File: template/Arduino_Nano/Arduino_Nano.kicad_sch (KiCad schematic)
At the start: 6 parts, among them P1 Digital, P2 Analog, P3 CONN_01X01, P4 CONN_01X01, P5 CONN_01X01, P6 CONN_01X01

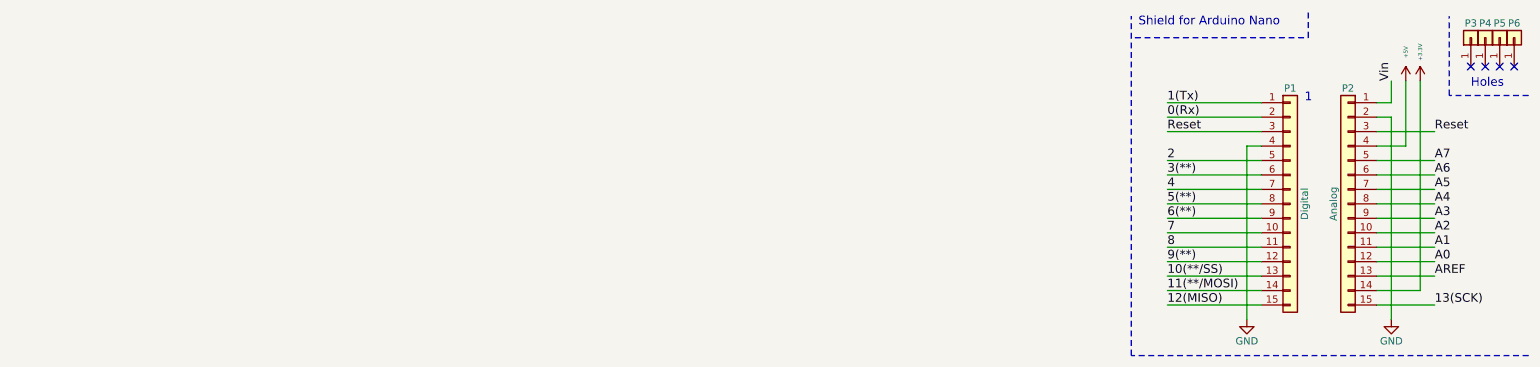
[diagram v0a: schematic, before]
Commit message: fix: change original libs; add: new components
- Fix LIS3DH pins positions;
- Add ATmega164P symbol;
- Add 3D model to the L_Wuerth_HCM-7050;
- Add parameters for R_RES (Assembly...).
- Add parameters for R_RES and C_CAP;
- Fix SOIC-8 package 3D model;
- Add new parameters for many symbols;
- Change text height from 70 mil to 50 mil;
- Add solder mask expansion for 2-contact jumpers;
- Change thermopad vias of QFN-20-1EP_3x3mm_P0.45mm_EP1.6x1.6mm_ThermalVias;
- Add D_SMAF footprint;
- Fillet silk for C_1206;
-Rectangle silk for R_1206;
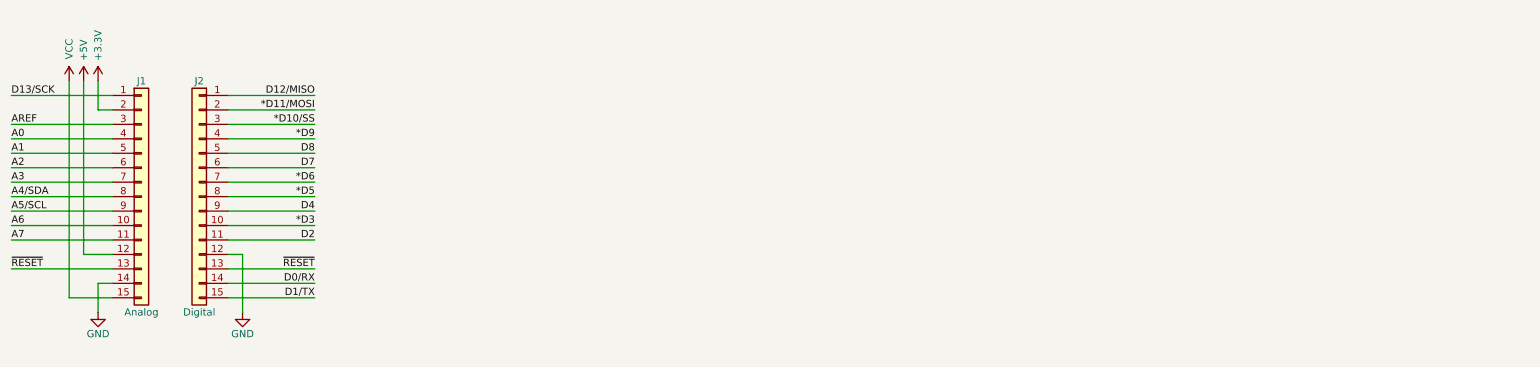
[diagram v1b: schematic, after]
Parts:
- removed P1: Digital, Socket_Arduino_Nano:Socket_Strip_Arduino_1x15, symbol Connector_Generic:Conn_01x15
- removed P2: Analog, Socket_Arduino_Nano:Socket_Strip_Arduino_1x15, symbol Connector_Generic:Conn_01x15
- removed P3, P4, P5, P6: CONN_01X01, Socket_Arduino_Nano:1pin_Nano, symbol Connector_Generic:Conn_01x01
- added J1: Analog, Connector_PinHeader_2.54mm:PinHeader_1x15_P2.54mm_Vertical, symbol Connector_Generic:Conn_01x15
- added J2: Digital, Connector_PinHeader_2.54mm:PinHeader_1x15_P2.54mm_Vertical, symbol Connector_Generic:Conn_01x15
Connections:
- net +3V3: now also J1.2 (Pin_2)
- net +5V: now also J1.12 (Pin_12)
- net A0: now also J1.4 (Pin_4)
- net A1: now also J1.5 (Pin_5)
- net A2: now also J1.6 (Pin_6)
- net A3: now also J1.7 (Pin_7)
- net A6: now also J1.10 (Pin_10)
- net A7: now also J1.11 (Pin_11)
- net AREF: now also J1.3 (Pin_3)
- net GND: now also J1.14 (Pin_14), J2.12 (Pin_12)
- new net *D10/SS: J2.3 (Pin_3)
- new net *D11/MOSI: J2.2 (Pin_2)
- new net *D3: J2.10 (Pin_10)
- new net *D5: J2.8 (Pin_8)
- new net *D6: J2.7 (Pin_7)
- new net *D9: J2.4 (Pin_4)
- new net A4/SDA: J1.8 (Pin_8)
- new net A5/SCL: J1.9 (Pin_9)
- new net D0/RX: J2.14 (Pin_14)
- new net D12/MISO: J2.1 (Pin_1)
- new net D13/SCK: J1.1 (Pin_1)
- new net D1/TX: J2.15 (Pin_15)
- new net D2: J2.11 (Pin_11)
- new net D4: J2.9 (Pin_9)
- new net D7: J2.6 (Pin_6)
- new net D8: J2.5 (Pin_5)
- new net VCC: J1.15 (Pin_15)
- new net ~{RESET}: J1.13 (Pin_13), J2.13 (Pin_13)
- no-connect marks 4 -> 0
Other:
- note removed: "1"
- note removed: "Holes"
- note removed: "Shield for Arduino Nano"
